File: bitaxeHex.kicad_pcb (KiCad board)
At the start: 4 copper layers, 84.5 x 129.5 mm, 372 parts, among them J1 Conn_01x01, J2 Conn_01x01, J3 Conn_02x05_Odd_Even, J4 TC2030-IDC, J5 Conn_01x04, J6 Conn_01x06, J7 USB_C_Receptacle_USB2.0, J8 Conn_01x04, J9 Conn_01x04, SW1 SWITCH-SPST, SW2 SWITCH-SPST, U1 LMR54410, U10 AP7331, U11 AP7331, U12 BM1368_mode1, U13 BM1368_mode0, U14 25MHz, U15 TLV3544, U16 AP7331, U17 AP7331, U18 BM1368_mode0, U19 25MHz, U2 RT9080-33GJ5, U21 TLV3544, U23 AP7331, U24 AP7331, U25 BM1368_mode1, U26 25MHz, U27 BM1368_mode1, U28 BM1368_mode1, U3 TPS546D24ARVFR, U4 MIC5504-MS, U5 SN74AVC4T774, U6 ESP32-S3-WROOM-1, U7 TMP1075, U8 TMP1075, U9 EMC2302, Y1 32.768kHz

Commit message: Add Logo
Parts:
- C34, C35: value 311-3342-1-ND -> 100nF

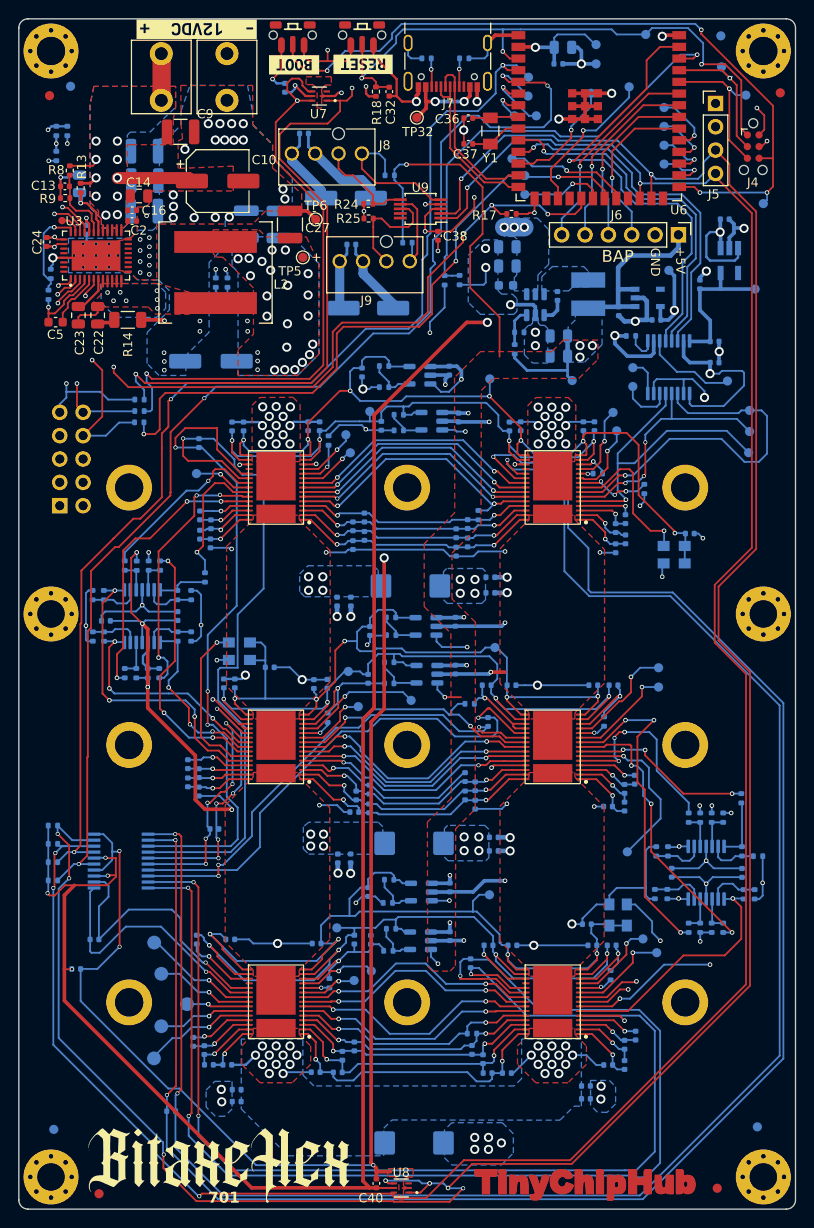
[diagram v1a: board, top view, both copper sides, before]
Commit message: Add TVS protection to avoid sudden current which may damage the TPS power regulator
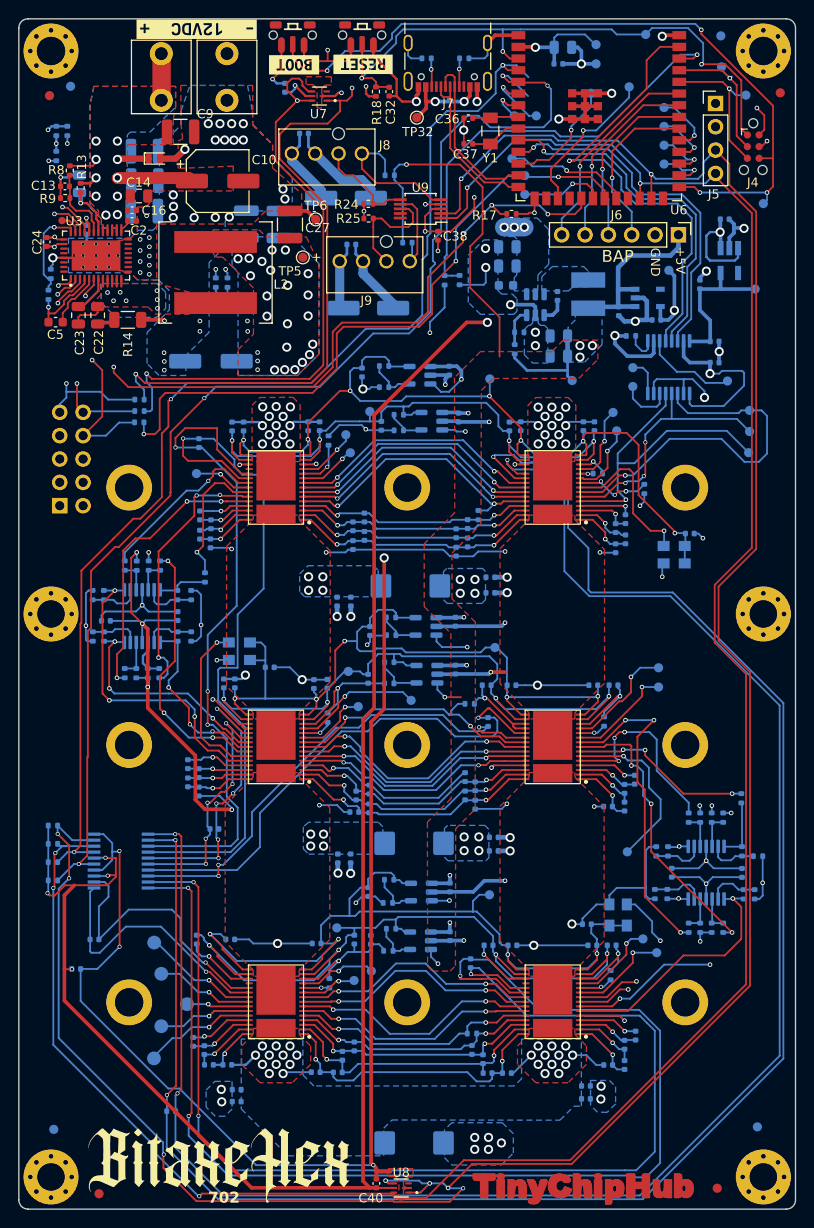
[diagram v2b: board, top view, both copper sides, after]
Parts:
- removed TP12, TP13: TestPoint, TestPoint:TestPoint_Pad_D1.0mm
- added D1: 824045812, bitaxe:824045812, F.Cu at (64.8, 61.2)
- C34, C35: value 100nF -> 311-3342-1-ND
- moved REF** 0.53 mm to (110.8, 174.0)
- moved REF** 0.47 mm to (110.8, 173.4)
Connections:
- C25 pad 1: /1V2 -> /Power/1V2
- C47 pad 1: BM1368-1/0V8 -> Net-(U28-VDDIO_08_0)
- C53 pad 1: BM1368-1/0V8 -> GND
- C58 pad 1: BM1368-1/0V8 -> GND
- C67 pad 1: BM1368-1/0V8 -> GND
- C76 pad 1: BM1368-1/0V8 -> GND
- R31 pad 2: BM1368-1/0V8 -> GND
- TP35 pad 1: BM1368-1/0V8 -> GND
- TP4 pad 1: /1V2 -> /Power/1V2
- U10 pad 5: BM1368-1/0V8 -> GND
- U12 pad 14: BM1368-1/0V8 -> GND
- U12 pad 17: BM1368-1/0V8 -> GND
- U28 pad 14: BM1368-1/0V8 -> Net-(U28-VDDIO_08_0)
- U28 pad 17: BM1368-1/0V8 -> GND
- U4 pad 5: /1V2 -> /Power/1V2
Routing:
- net GND: track 374.0 -> 446.5 mm, vias 110 -> 114
- net BM1368-1/0V8: track 69.4 -> 0.00 mm, vias 4 -> 0
- net /VIN: track 111.7 -> 115.2 mm
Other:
- board text added: "702"
- board text removed: "701"

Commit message: minor
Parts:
- C40: value 311-3342-1-ND -> 0.1uF
